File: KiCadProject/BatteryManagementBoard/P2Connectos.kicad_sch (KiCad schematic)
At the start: 19 parts, among them J201 USB-C-2.0, J202 XT30, J203 Conn_02x05, J204 XT60, J205 Conn_02x05, J206 Conn_01x02_Male, J207 Conn_01x05_Male, J208 JST_B5B_XH

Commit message: Layout on the battery management board
Signed-off-by: Eldalote.Electronics <Eldalote.Electronics@gmail.com>
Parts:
- removed TP202, TP203, TP204, TP209, TP210: TestPoint, TestPoint:TestPoint_Pad_D1.0mm, symbol Connector:TestPoint
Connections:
- net +3V3 renamed +3.3V

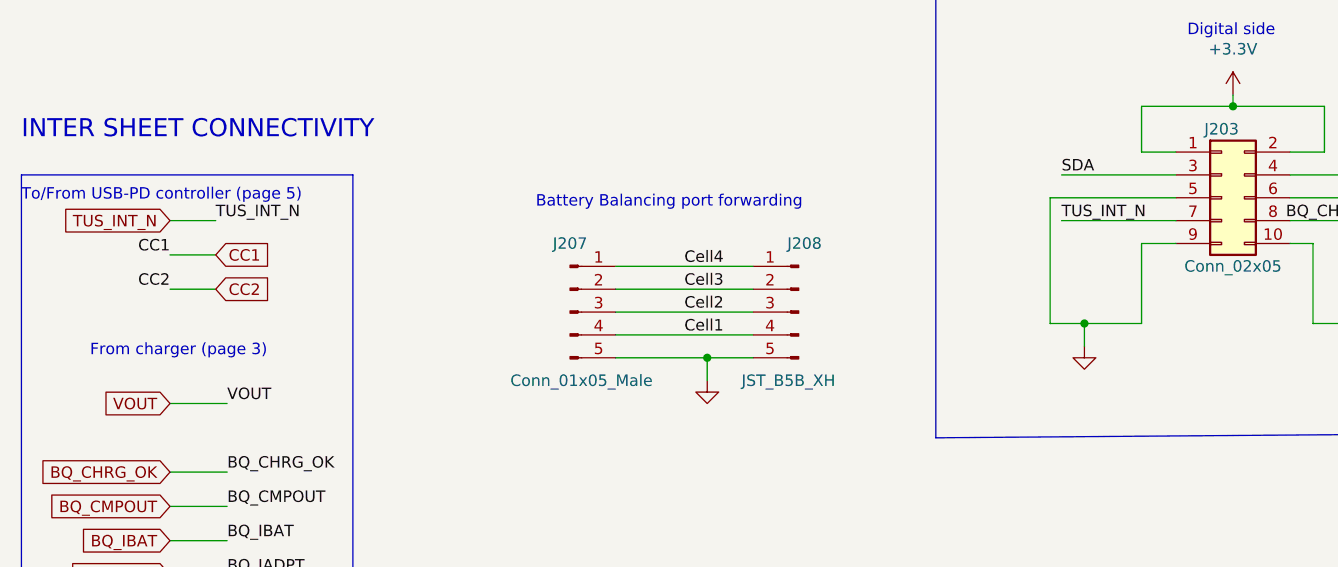
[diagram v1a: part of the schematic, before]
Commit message: Routed Bat management (replaced TUSB because it physically can't be routed with constraints)
Signed-off-by: Eldalote.Electronics <Eldalote.Electronics@gmail.com>
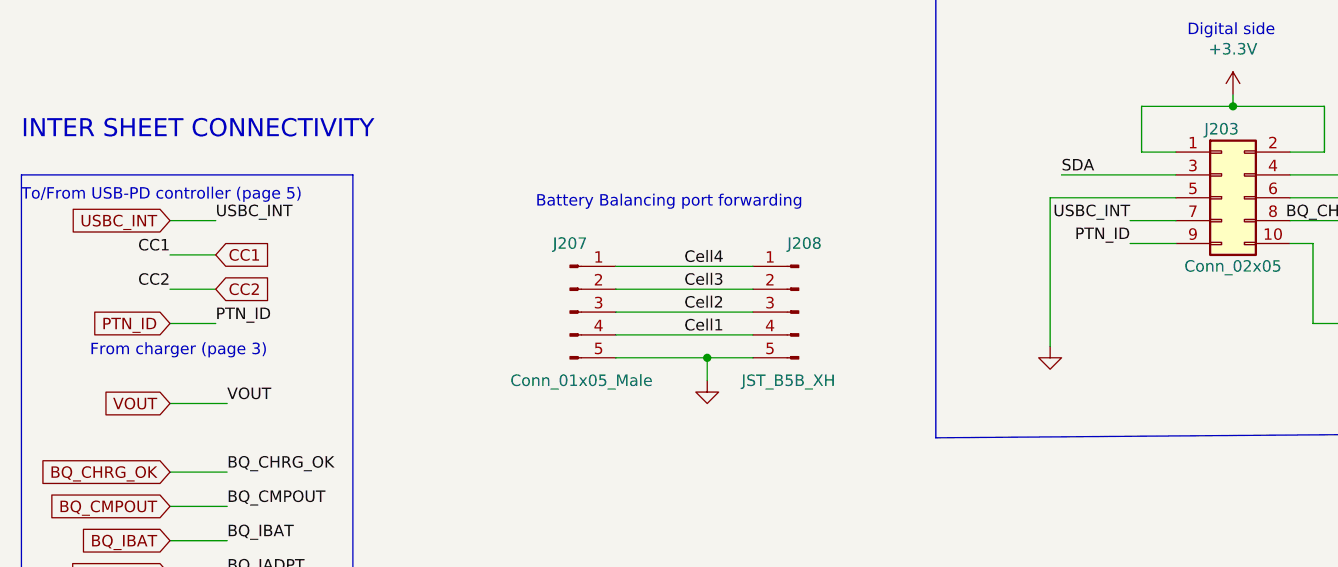
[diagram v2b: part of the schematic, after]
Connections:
- net GND: no longer J203.9 (Pin_9)
- net TUS_INT_N renamed USBC_INT
- new net PTN_ID: J203.9 (Pin_9)

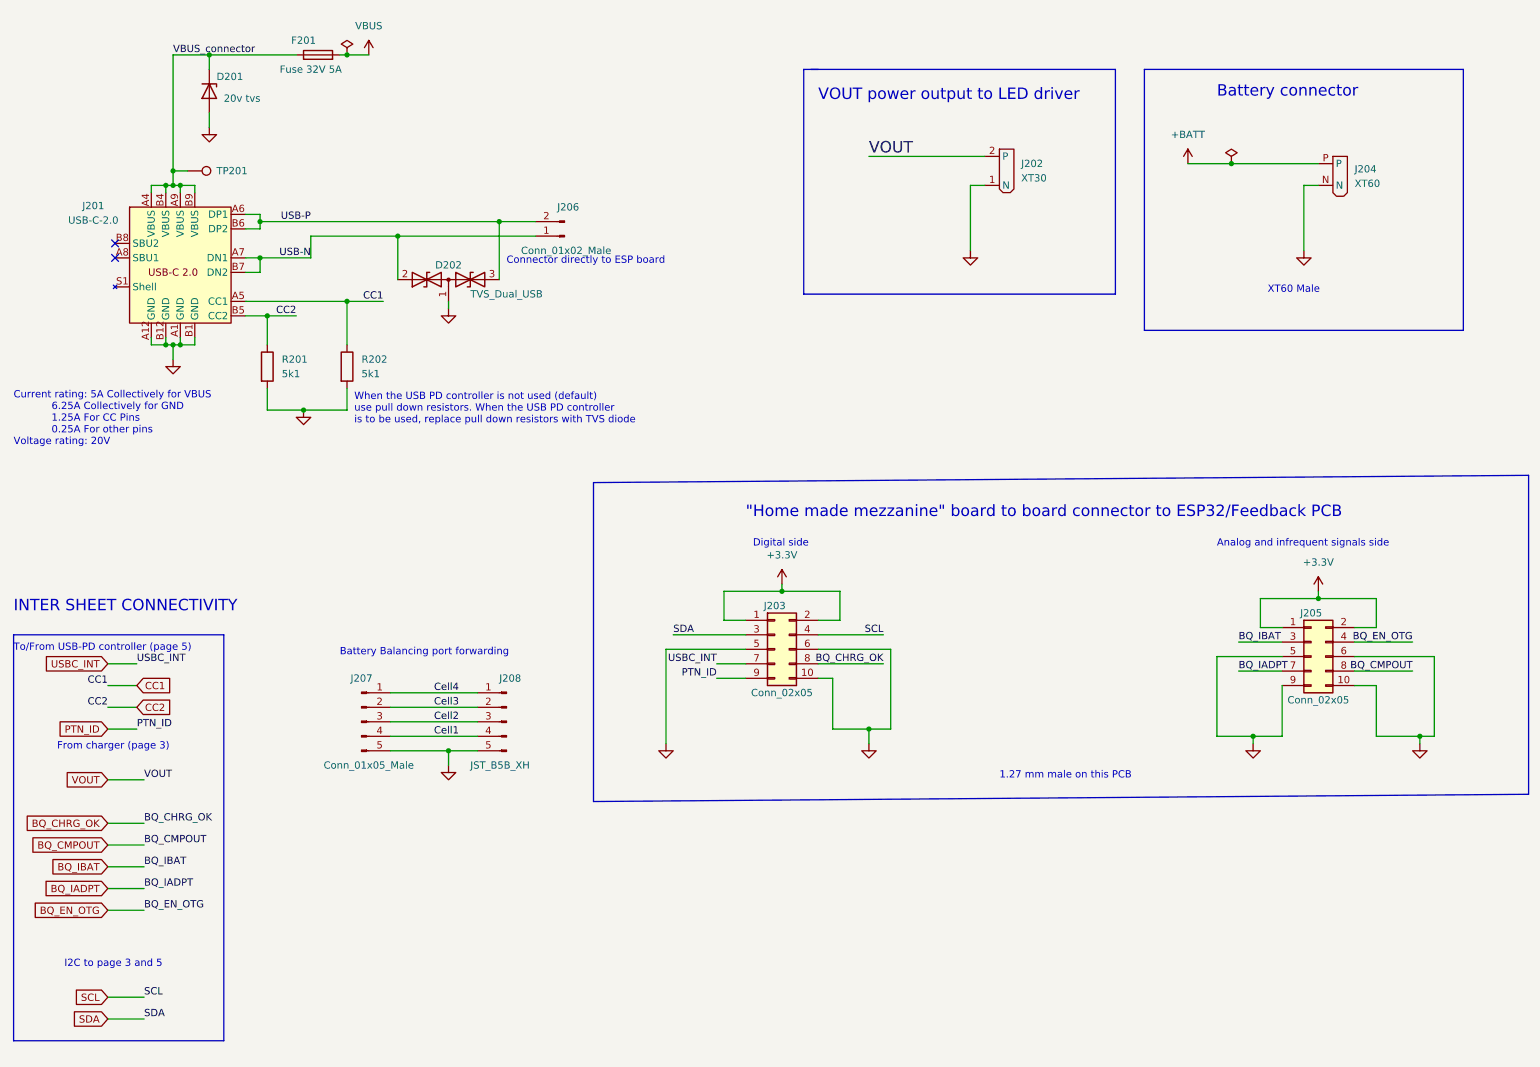
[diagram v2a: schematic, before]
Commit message: All PCB's should be done. Do a final check before ordering.
Signed-off-by: Eldalote.Electronics <Eldalote.Electronics@gmail.com>
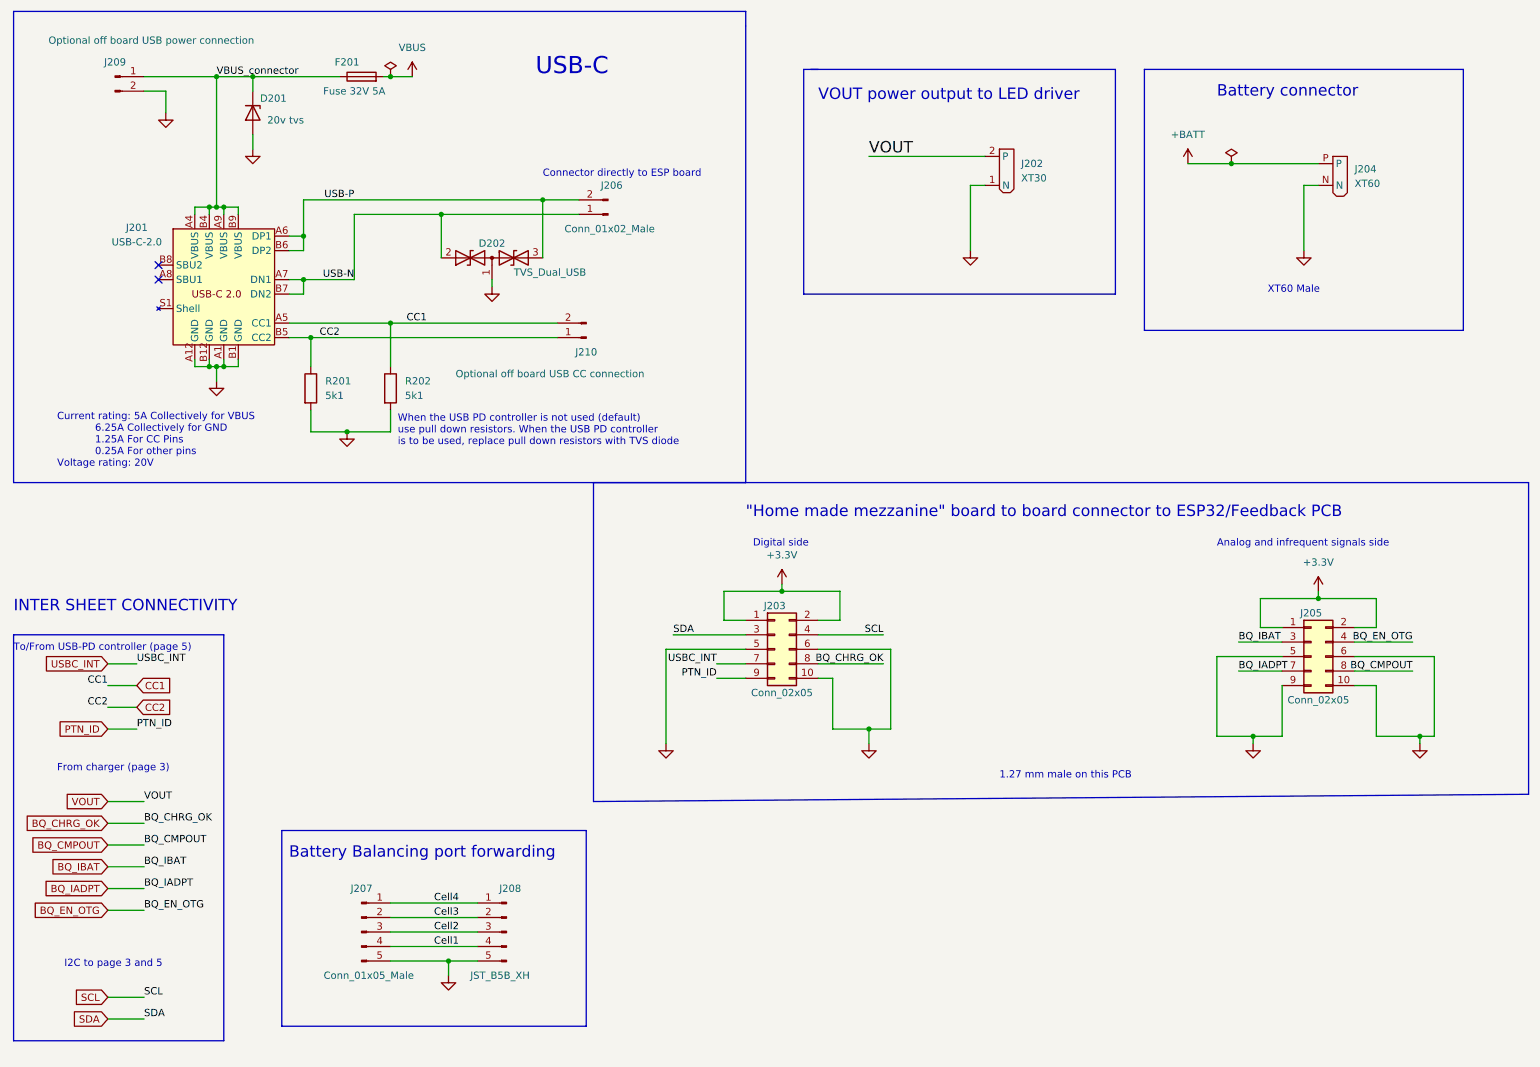
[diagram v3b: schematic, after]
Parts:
- removed TP201: TestPoint, TestPoint:TestPoint_Pad_D1.0mm, symbol Connector:TestPoint
- added J209: Optional off board USB power connection, Connector_PinHeader_2.00mm:PinHeader_1x02_P2.00mm_Vertical, symbol Connector:Conn_01x02_Male
- added J210: Optional off board USB CC connection, Connector_PinHeader_1.00mm:PinHeader_1x02_P1.00mm_Vertical, symbol Connector:Conn_01x02_Male
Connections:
- net CC1: now also J210.2 (Pin_2)
- net CC2: now also J210.1 (Pin_1)
- net GND: now also J209.2 (Pin_2)
- net VBUS_connector: now also J209.1 (Pin_1)
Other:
- note added: "USB-C"
- moved on the sheet: D201, D202, F201, J201, J206, J207, J208, R201, R202

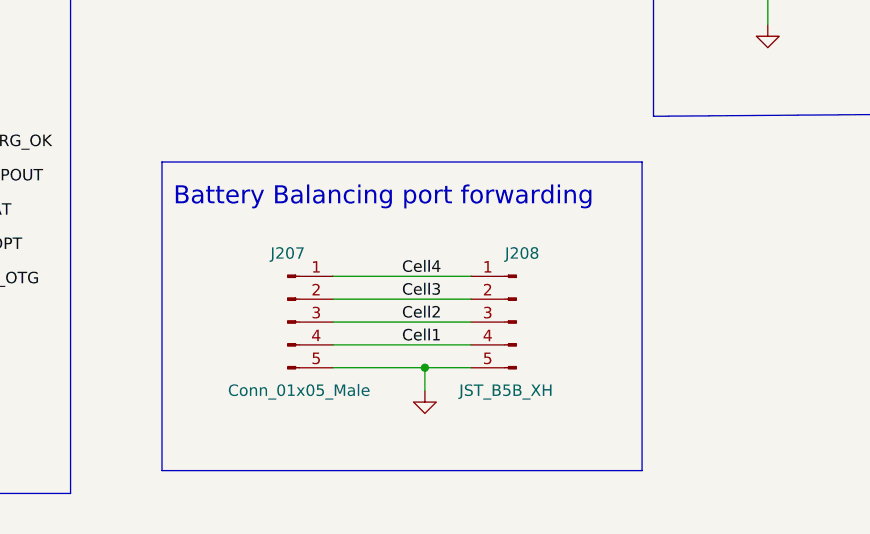
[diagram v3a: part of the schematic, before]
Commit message: Made ready to order PCBs. Some problems with ordering due to misunderstanding. Thinking about solutions
Signed-off-by: Eldalote.Electronics <Eldalote.Electronics@gmail.com>
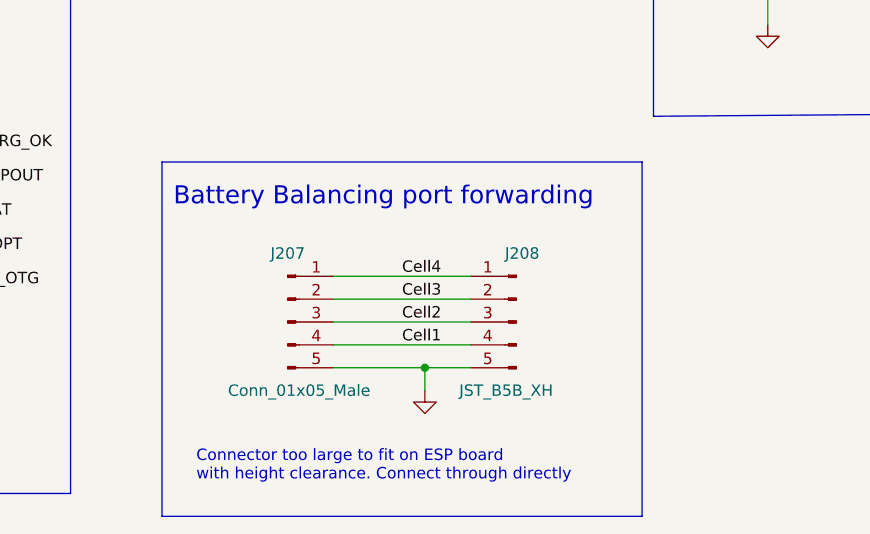
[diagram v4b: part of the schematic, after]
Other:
- note added: "Connector too large to fit on ESP board with height clearance. Connect through directly"
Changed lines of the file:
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@@
     (stroke (width 0) (type default) (color 0 0 0 0))
   )
-  (polyline (pts (xy 63.5 191.77) (xy 63.5 157.48))
+  (polyline (pts (xy 63.5 196.85) (xy 63.5 157.48))
     (stroke (width 0) (type default) (color 0 0 0 0))
   )
@@
     (stroke (width 0) (type default) (color 0 0 0 0))
   )
-  (polyline (pts (xy 116.84 191.77) (xy 63.5 191.77))
+  (polyline (pts (xy 116.84 196.85) (xy 63.5 196.85))
     (stroke (width 0) (type default) (color 0 0 0 0))
   )
@@
     (stroke (width 0) (type default) (color 0 0 0 0))
   )
-  (polyline (pts (xy 116.84 157.48) (xy 116.84 191.77))
+  (polyline (pts (xy 116.84 157.48) (xy 116.84 196.85))
     (stroke (width 0) (type default) (color 0 0 0 0))
   )
@@
     (effects (font (size 1.27 1.27)) (justify left bottom))
   )
+  (text "Connector too large to fit on ESP board \nwith height clearance. Connect through directly"
+    (at 67.31 193.04 0)
+    (effects (font (size 1.27 1.27)) (justify left bottom))
+  )
